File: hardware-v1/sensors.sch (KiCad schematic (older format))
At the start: 13 parts, among them U13 BMP280, U14 BNO055, U15 MPL3115A2

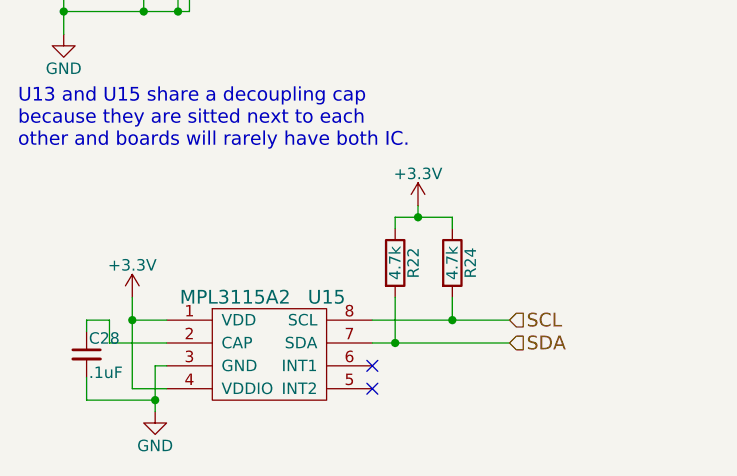
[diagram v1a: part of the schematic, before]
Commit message: remove mpl3115a2 barometer (keep bmp280)
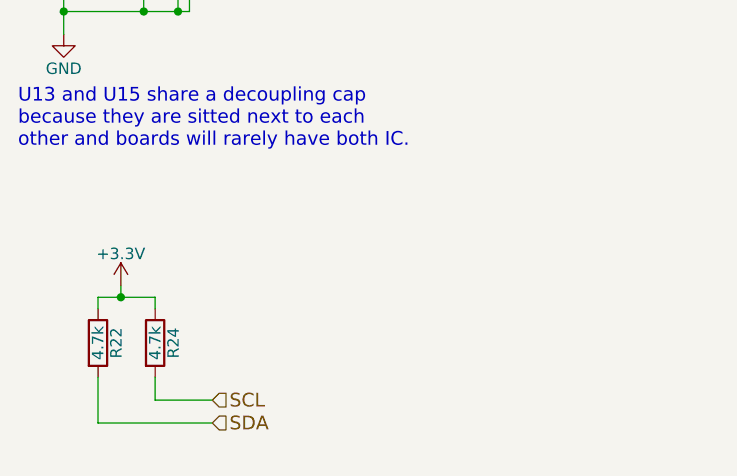
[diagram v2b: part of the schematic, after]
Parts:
- removed C28: .1uF, Capacitors_SMD:C_0603_HandSoldering, symbol C_Small
- removed U15: MPL3115A2, bb:MPL3115A2, symbol MPL3115A2
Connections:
- no-connect marks 13 -> 11
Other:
- moved on the sheet: R22, R24
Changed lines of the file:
@@
 Wire Wire Line
 	2850 1700 2900 1700
-$Comp
-L MPL3115A2 U15
-U 1 1 566E0CBC
-P 2300 3500
-F 0 "U15" H 2550 3750 60  0000 C CNN
-F 1 "MPL3115A2" H 2150 3750 60  0000 C CNN
-F 2 "bb:MPL3115A2" H 2300 3500 60  0001 C CNN
-F 3 "" H 2300 3500 60  0000 C CNN
-	1    2300 3500
-	1    0    0    -1
-$EndComp
-$Comp
-L C_Small C28
-U 1 1 566E0CC3
-P 1500 3500
-F 0 "C28" H 1510 3570 50  0000 L CNN
-F 1 ".1uF" H 1510 3420 50  0000 L CNN
-F 2 "Capacitors_SMD:C_0603_HandSoldering" H 1500 3500 60  0001 C CNN
-F 3 "" H 1500 3500 60  0000 C CNN
-	1    1500 3500
-	1    0    0    -1
-$EndComp
-NoConn ~ 2750 3550
-NoConn ~ 2750 3650
-$Comp
-L +3.3V #PWR077
-U 1 1 566E0CD5
-P 1700 3250
-F 0 "#PWR077" H 1700 3100 50  0001 C CNN
-F 1 "+3.3V" H 1700 3390 50  0000 C CNN
-F 2 "" H 1700 3250 60  0000 C CNN
-F 3 "" H 1700 3250 60  0000 C CNN
-	1    1700 3250
-	1    0    0    -1
-$EndComp
-Wire Wire Line
-	1700 3250 1700 3650
-Wire Wire Line
-	1700 3350 1850 3350
-Wire Wire Line
-	1700 3650 1850 3650
-Connection ~ 1700 3350
-Wire Wire Line
-	1850 3550 1800 3550
-Wire Wire Line
-	1800 3550 1800 3750
-$Comp
-L GND #PWR078
-U 1 1 566E0CE1
-P 1800 3750
-F 0 "#PWR078" H 1800 3500 50  0001 C CNN
-F 1 "GND" H 1800 3600 50  0000 C CNN
-F 2 "" H 1800 3750 60  0000 C CNN
-F 3 "" H 1800 3750 60  0000 C CNN
-	1    1800 3750
-	1    0    0    -1
-$EndComp
-Connection ~ 1800 3700
-Wire Wire Line
-	1500 3600 1500 3700
-Wire Wire Line
-	1600 3450 1850 3450
-Wire Wire Line
-	1600 3350 1600 3450
-Wire Wire Line
-	1600 3350 1500 3350
-Wire Wire Line
-	1500 3350 1500 3400
 Connection ~ 1400 2000
-Wire Wire Line
-	2750 3350 3350 3350
-Wire Wire Line
-	2750 3450 3350 3450
 $Comp
 L R R22
 U 1 1 566E0CF6
-P 2850 3100
-F 0 "R22" V 2930 3100 50  0000 C CNN
-F 1 "4.7k" V 2850 3100 50  0000 C CNN
-F 2 "Resistors_SMD:R_0603_HandSoldering" V 2780 3100 30  0001 C CNN
-F 3 "" H 2850 3100 30  0000 C CNN
-	1    2850 3100
+P 1550 3450
+F 0 "R22" V 1630 3450 50  0000 C CNN
+F 1 "4.7k" V 1550 3450 50  0000 C CNN
+F 2 "Resistors_SMD:R_0603_HandSoldering" V 1480 3450 30  0001 C CNN
+F 3 "" H 1550 3450 30  0000 C CNN
+	1    1550 3450
 	1    0    0    -1
 $EndComp
@@
 L R R24
 U 1 1 566E0CFD
-P 3100 3100
-F 0 "R24" V 3180 3100 50  0000 C CNN
-F 1 "4.7k" V 3100 3100 50  0000 C CNN
-F 2 "Resistors_SMD:R_0603_HandSoldering" V 3030 3100 30  0001 C CNN
-F 3 "" H 3100 3100 30  0000 C CNN
-	1    3100 3100
-	1    0    0    -1
-$EndComp
-Wire Wire Line
-	2850 3250 2850 3450
-Connection ~ 2850 3450
-Wire Wire Line
-	3100 3250 3100 3350
-Connection ~ 3100 3350
-Wire Wire Line
-	3100 2900 3100 2950
-Wire Wire Line
-	2850 2950 2850 2900
-Wire Wire Line
-	2850 2900 3100 2900
+P 1800 3450
+F 0 "R24" V 1880 3450 50  0000 C CNN
+F 1 "4.7k" V 1800 3450 50  0000 C CNN
+F 2 "Resistors_SMD:R_0603_HandSoldering" V 1730 3450 30  0001 C CNN
+F 3 "" H 1800 3450 30  0000 C CNN
+	1    1800 3450
+	1    0    0    -1
+$EndComp
+Wire Wire Line
+	1550 3600 1550 3800
+Wire Wire Line
+	1800 3600 1800 3700
+Wire Wire Line
+	1800 3250 1800 3300
+Wire Wire Line
+	1550 3300 1550 3250
+Wire Wire Line
+	1550 3250 1800 3250
 $Comp
 L +3.3V #PWR079
 U 1 1 566E0D0B
-P 2950 2850
-F 0 "#PWR079" H 2950 2700 50  0001 C CNN
-F 1 "+3.3V" H 2950 2990 50  0000 C CNN
-F 2 "" H 2950 2850 60  0000 C CNN
-F 3 "" H 2950 2850 60  0000 C CNN
-	1    2950 2850
-	1    0    0    -1
-$EndComp
-Wire Wire Line
-	2950 2850 2950 2900
-Connection ~ 2950 2900
-Text HLabel 3350 3350 2    60   Input ~ 0
+P 1650 3200
+F 0 "#PWR079" H 1650 3050 50  0001 C CNN
+F 1 "+3.3V" H 1650 3340 50  0000 C CNN
+F 2 "" H 1650 3200 60  0000 C CNN
+F 3 "" H 1650 3200 60  0000 C CNN
+	1    1650 3200
+	1    0    0    -1
+$EndComp
+Wire Wire Line
+	1650 3200 1650 3250
+Connection ~ 1650 3250
+Text HLabel 2050 3700 2    60   Input ~ 0
 SCL
-Text HLabel 3350 3450 2    60   Input ~ 0
+Text HLabel 2050 3800 2    60   Input ~ 0
 SDA
 Text HLabel 2900 1600 2    60   Input ~ 0
@@
 U13 and U15 share a decoupling cap \nbecause they are sitted next to each \nother and boards will rarely have both IC.
 Wire Wire Line
-	1500 3700 1800 3700
-Wire Wire Line
 	1400 1400 1950 1400
 Wire Wire Line
 	1400 2000 1950 2000
+Wire Wire Line
+	1800 3700 2050 3700
+Wire Wire Line
+	1550 3800 2050 3800
 $EndSCHEMATC

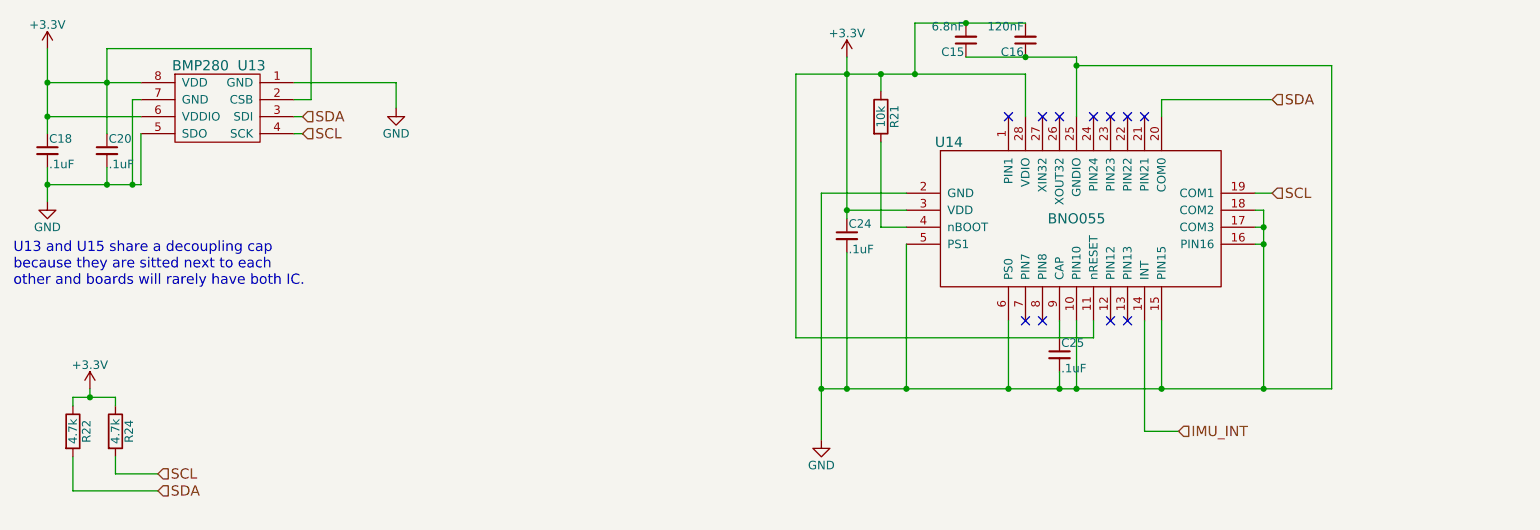
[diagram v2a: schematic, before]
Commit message: Add i2c addresses on schematic
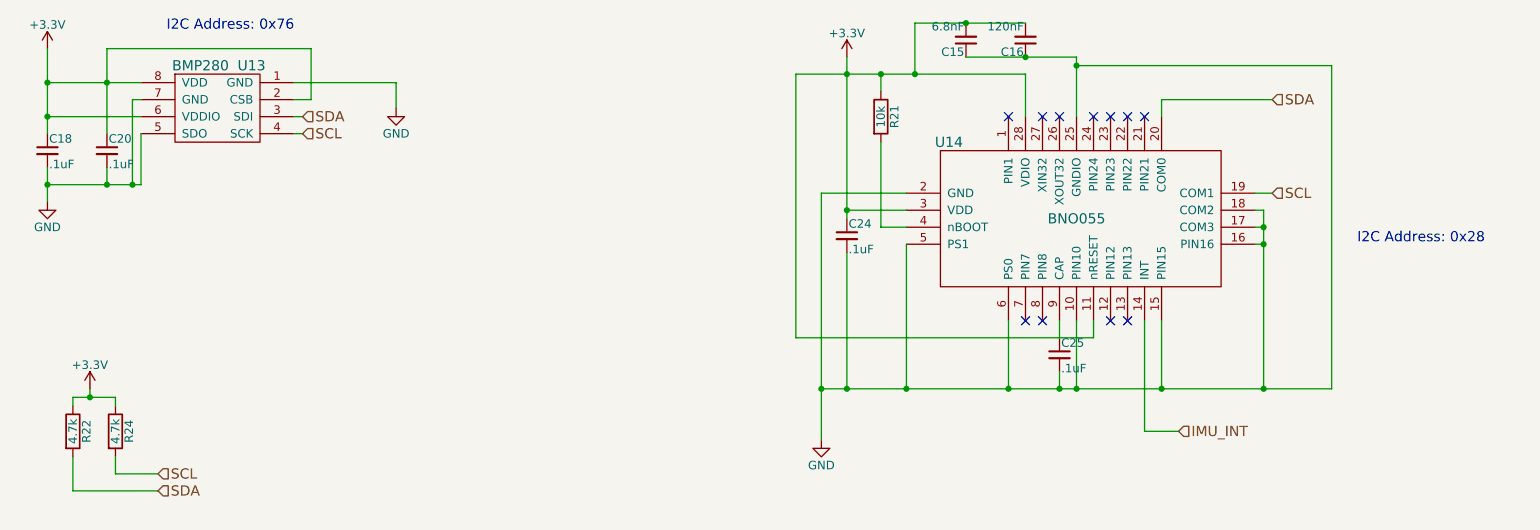
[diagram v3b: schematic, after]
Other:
- note added: "I2C Address: 0x28"
- note added: "I2C Address: 0x76"
- note removed: "U13 and U15 share a decoupling cap \nbecause they are sitted next to each \nother and boards will rarely have both IC."
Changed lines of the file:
@@
 NoConn ~ 7250 1600
 NoConn ~ 7350 1600
-Text Notes 1200 2600 0    60   ~ 0
-U13 and U15 share a decoupling cap \nbecause they are sitted next to each \nother and boards will rarely have both IC.
 Wire Wire Line
 	1400 1400 1950 1400
@@
 Wire Wire Line
 	1550 3800 2050 3800
+Text Notes 2100 1100 0    60   ~ 0
+I2C Address: 0x76
+Text Notes 9100 2350 0    60   ~ 0
+I2C Address: 0x28
 $EndSCHEMATC

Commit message: Connect IMU_RESET to teensy
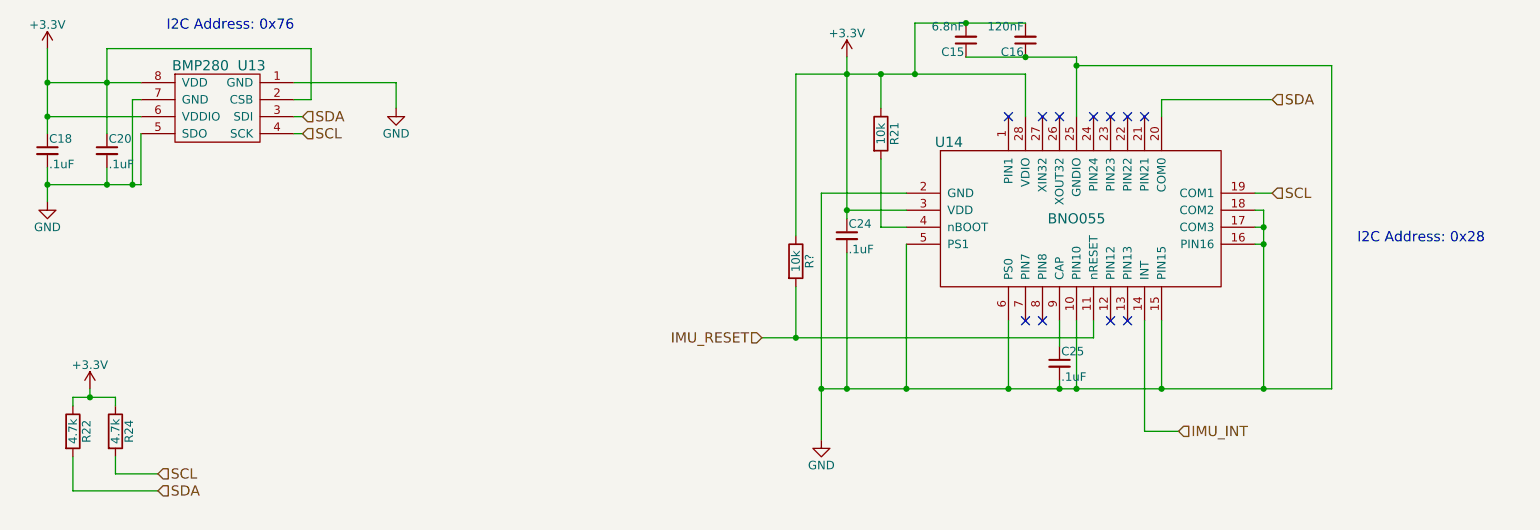
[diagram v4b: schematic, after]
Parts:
- added R?: 10k, Resistors_SMD:R_0603_HandSoldering, symbol R
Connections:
- net +3V3: now also R?.1; no longer U14.11 (nRESET)
- new net IMU_RESET: R?.2, U14.11 (nRESET)
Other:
- moved on the sheet: C25, R21
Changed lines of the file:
@@
 $EndComp
 Wire Wire Line
-	1400 1200 1400 1700
+	1400 1200 1400 1400
+Wire Wire Line
+	1400 1400 1400 1600
+Wire Wire Line
+	1400 1600 1400 1700
 Wire Wire Line
 	1400 1600 1950 1600
@@
 $EndComp
 Wire Wire Line
-	1750 1200 1750 1700
+	1750 1200 1750 1400
+Wire Wire Line
+	1750 1400 1750 1700
 Connection ~ 1750 1400
 Connection ~ 1400 1600
 Wire Wire Line
-	1400 1900 1400 2100
+	1400 1900 1400 2000
+Wire Wire Line
+	1400 2000 1400 2100
 Wire Wire Line
 	1750 1900 1750 2000
@@
 	1550 3300 1550 3250
 Wire Wire Line
-	1550 3250 1800 3250
+	1550 3250 1650 3250
+Wire Wire Line
+	1650 3250 1800 3250
 $Comp
 L +3.3V #PWR079
@@
 	6450 2050 5950 2050
 Wire Wire Line
-	5950 2050 5950 3500
+	5950 2050 5950 3200
+Wire Wire Line
+	5950 3200 5950 3500
 NoConn ~ 7050 1600
 $Comp
@@
 	6100 2150 6450 2150
 Wire Wire Line
-	6100 1250 6100 2200
+	6100 1250 6100 1350
+Wire Wire Line
+	6100 1350 6100 2150
+Wire Wire Line
+	6100 2150 6100 2200
 $Comp
 L +3.3V #PWR081
@@
 	6450 2250 6300 2250
 Wire Wire Line
-	6300 2250 6300 1750
+	6300 2250 6300 1850
 $Comp
 L R R21
 U 1 1 566E34C5
-P 6300 1600
-F 0 "R21" V 6380 1600 50  0000 C CNN
-F 1 "10k" V 6300 1600 50  0000 C CNN
-F 2 "Resistors_SMD:R_0603_HandSoldering" V 6230 1600 30  0001 C CNN
-F 3 "" H 6300 1600 30  0000 C CNN
-	1    6300 1600
-	1    0    0    -1
-$EndComp
-Wire Wire Line
-	6300 1350 6300 1450
-Wire Wire Line
-	5800 1350 7150 1350
+P 6300 1700
+F 0 "R21" V 6380 1700 50  0000 C CNN
+F 1 "10k" V 6300 1700 50  0000 C CNN
+F 2 "Resistors_SMD:R_0603_HandSoldering" V 6230 1700 30  0001 C CNN
+F 3 "" H 6300 1700 30  0000 C CNN
+	1    6300 1700
+	1    0    0    -1
+$EndComp
+Wire Wire Line
+	6300 1350 6300 1550
+Wire Wire Line
+	5800 1350 6100 1350
+Wire Wire Line
+	6100 1350 6300 1350
+Wire Wire Line
+	6300 1350 6500 1350
+Wire Wire Line
+	6500 1350 7150 1350
 Connection ~ 6100 1350
 Wire Wire Line
@@
 L C_Small C25
 U 1 1 566E365A
-P 7350 3000
-F 0 "C25" H 7360 3070 50  0000 L CNN
-F 1 ".1uF" H 7360 2920 50  0000 L CNN
-F 2 "Capacitors_SMD:C_0603_HandSoldering" H 7350 3000 60  0001 C CNN
-F 3 "" H 7350 3000 60  0000 C CNN
-	1    7350 3000
-	1    0    0    -1
-$EndComp
-Wire Wire Line
-	7350 2800 7350 2900
+P 7350 3050
+F 0 "C25" H 7360 3120 50  0000 L CNN
+F 1 ".1uF" H 7360 2970 50  0000 L CNN
+F 2 "Capacitors_SMD:C_0603_HandSoldering" H 7350 3050 60  0001 C CNN
+F 3 "" H 7350 3050 60  0000 C CNN
+	1    7350 3050
+	1    0    0    -1
+$EndComp
+Wire Wire Line
+	7350 2800 7350 2950
 Wire Wire Line
 	7450 3200 7450 2800
 Wire Wire Line
-	5950 3200 8950 3200
-Wire Wire Line
-	7350 3200 7350 3100
+	5950 3200 6100 3200
+Wire Wire Line
+	6100 3200 6450 3200
+Wire Wire Line
+	6450 3200 7050 3200
+Wire Wire Line
+	7050 3200 7350 3200
+Wire Wire Line
+	7350 3200 7450 3200
+Wire Wire Line
+	7450 3200 7950 3200
+Wire Wire Line
+	7950 3200 8550 3200
+Wire Wire Line
+	8550 3200 8950 3200
+Wire Wire Line
+	7350 3200 7350 3150
 Connection ~ 5950 3200
 Connection ~ 7350 3200
@@
 Connection ~ 6450 3200
 Wire Wire Line
-	7550 2800 7550 2900
-Wire Wire Line
-	7550 2900 5800 2900
-Wire Wire Line
-	5800 2900 5800 1350
+	7550 2900 7550 2800
+Wire Wire Line
+	5600 2900 5800 2900
+Wire Wire Line
+	5800 2900 7550 2900
 NoConn ~ 7650 2800
 NoConn ~ 7750 2800
@@
 	8550 2350 8500 2350
 Wire Wire Line
-	8550 2150 8550 3200
+	8550 2150 8550 2250
+Wire Wire Line
+	8550 2250 8550 2350
+Wire Wire Line
+	8550 2350 8550 3200
 Connection ~ 7950 3200
 Wire Wire Line
@@
 NoConn ~ 7550 1600
 Wire Wire Line
-	7450 1250 7450 1600
+	7450 1250 7450 1300
+Wire Wire Line
+	7450 1300 7450 1600
 Wire Wire Line
 	7450 1300 8950 1300
@@
 $EndComp
 Wire Wire Line
-	6500 1050 7150 1050
+	6500 1050 6800 1050
+Wire Wire Line
+	6800 1050 7150 1050
 Wire Wire Line
 	6500 1050 6500 1350
@@
 Connection ~ 6800 1050
 Wire Wire Line
-	6800 1250 7450 1250
+	6800 1250 7150 1250
+Wire Wire Line
+	7150 1250 7450 1250
 Connection ~ 7450 1300
 Connection ~ 7150 1250
@@
 NoConn ~ 7350 1600
 Wire Wire Line
-	1400 1400 1950 1400
-Wire Wire Line
-	1400 2000 1950 2000
+	1400 1400 1750 1400
+Wire Wire Line
+	1750 1400 1950 1400
+Wire Wire Line
+	1400 2000 1750 2000
+Wire Wire Line
+	1750 2000 1900 2000
+Wire Wire Line
+	1900 2000 1950 2000
 Wire Wire Line
 	1800 3700 2050 3700
@@
 Text Notes 9100 2350 0    60   ~ 0
 I2C Address: 0x28
+Text HLabel 5600 2900 0    60   Input ~ 0
+IMU_RESET
+Connection ~ 5800 2900
+$Comp
+L R R?
+U 1 1 56A47B87
+P 5800 2450
+F 0 "R?" V 5880 2450 50  0000 C CNN
+F 1 "10k" V 5800 2450 50  0000 C CNN
+F 2 "Resistors_SMD:R_0603_HandSoldering" V 5730 2450 30  0001 C CNN
+F 3 "" H 5800 2450 30  0000 C CNN
+	1    5800 2450
+	1    0    0    -1
+$EndComp
+Wire Wire Line
+	5800 2600 5800 2900
+Wire Wire Line
+	5800 2300 5800 1350
 $EndSCHEMATC

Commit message: re-annotate schematic
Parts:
- gave numbers to parts that had none: 1
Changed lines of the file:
@@
 Connection ~ 1400 1400
 $Comp
-L +3.3V #PWR074
+L +3.3V #PWR64
 U 1 1 566E0C88
 P 1400 1200
-F 0 "#PWR074" H 1400 1050 50  0001 C CNN
+F 0 "#PWR64" H 1400 1050 50  0001 C CNN
 F 1 "+3.3V" H 1400 1340 50  0000 C CNN
 F 2 "" H 1400 1200 60  0000 C CNN
@@
 Connection ~ 1900 2000
 $Comp
-L GND #PWR075
+L GND #PWR67
 U 1 1 566E0CA7
 P 1400 2100
-F 0 "#PWR075" H 1400 1850 50  0001 C CNN
+F 0 "#PWR67" H 1400 1850 50  0001 C CNN
 F 1 "GND" H 1400 1950 50  0000 C CNN
 F 2 "" H 1400 2100 60  0000 C CNN
@@
 	3450 1400 3450 1550
 $Comp
-L GND #PWR076
+L GND #PWR66
 U 1 1 566E0CAF
 P 3450 1550
-F 0 "#PWR076" H 3450 1300 50  0001 C CNN
+F 0 "#PWR66" H 3450 1300 50  0001 C CNN
 F 1 "GND" H 3450 1400 50  0000 C CNN
 F 2 "" H 3450 1550 60  0000 C CNN
@@
 	1650 3250 1800 3250
 $Comp
-L +3.3V #PWR079
+L +3.3V #PWR68
 U 1 1 566E0D0B
 P 1650 3200
-F 0 "#PWR079" H 1650 3050 50  0001 C CNN
+F 0 "#PWR68" H 1650 3050 50  0001 C CNN
 F 1 "+3.3V" H 1650 3340 50  0000 C CNN
 F 2 "" H 1650 3200 60  0000 C CNN
@@
 NoConn ~ 7050 1600
 $Comp
-L GND #PWR080
+L GND #PWR69
 U 1 1 566E19B5
 P 5950 3500
-F 0 "#PWR080" H 5950 3250 50  0001 C CNN
+F 0 "#PWR69" H 5950 3250 50  0001 C CNN
 F 1 "GND" H 5950 3350 50  0000 C CNN
 F 2 "" H 5950 3500 60  0000 C CNN
@@
 	6100 2150 6100 2200
 $Comp
-L +3.3V #PWR081
+L +3.3V #PWR65
 U 1 1 566E28E8
 P 6100 1250
-F 0 "#PWR081" H 6100 1100 50  0001 C CNN
+F 0 "#PWR65" H 6100 1100 50  0001 C CNN
 F 1 "+3.3V" H 6100 1390 50  0000 C CNN
 F 2 "" H 6100 1250 60  0000 C CNN
@@
 Connection ~ 5800 2900
 $Comp
-L R R?
+L R R27
 U 1 1 56A47B87
 P 5800 2450
-F 0 "R?" V 5880 2450 50  0000 C CNN
+F 0 "R27" V 5880 2450 50  0000 C CNN
 F 1 "10k" V 5800 2450 50  0000 C CNN
 F 2 "Resistors_SMD:R_0603_HandSoldering" V 5730 2450 30  0001 C CNN
